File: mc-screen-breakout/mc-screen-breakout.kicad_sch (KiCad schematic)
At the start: 25 parts, among them J1 USB_C_Receptacle_PowerOnly_6P, J2 FH28-10S-0.5SH_05_, U2 MDBT50Q-1MV2, Y1 Crystal_GND24

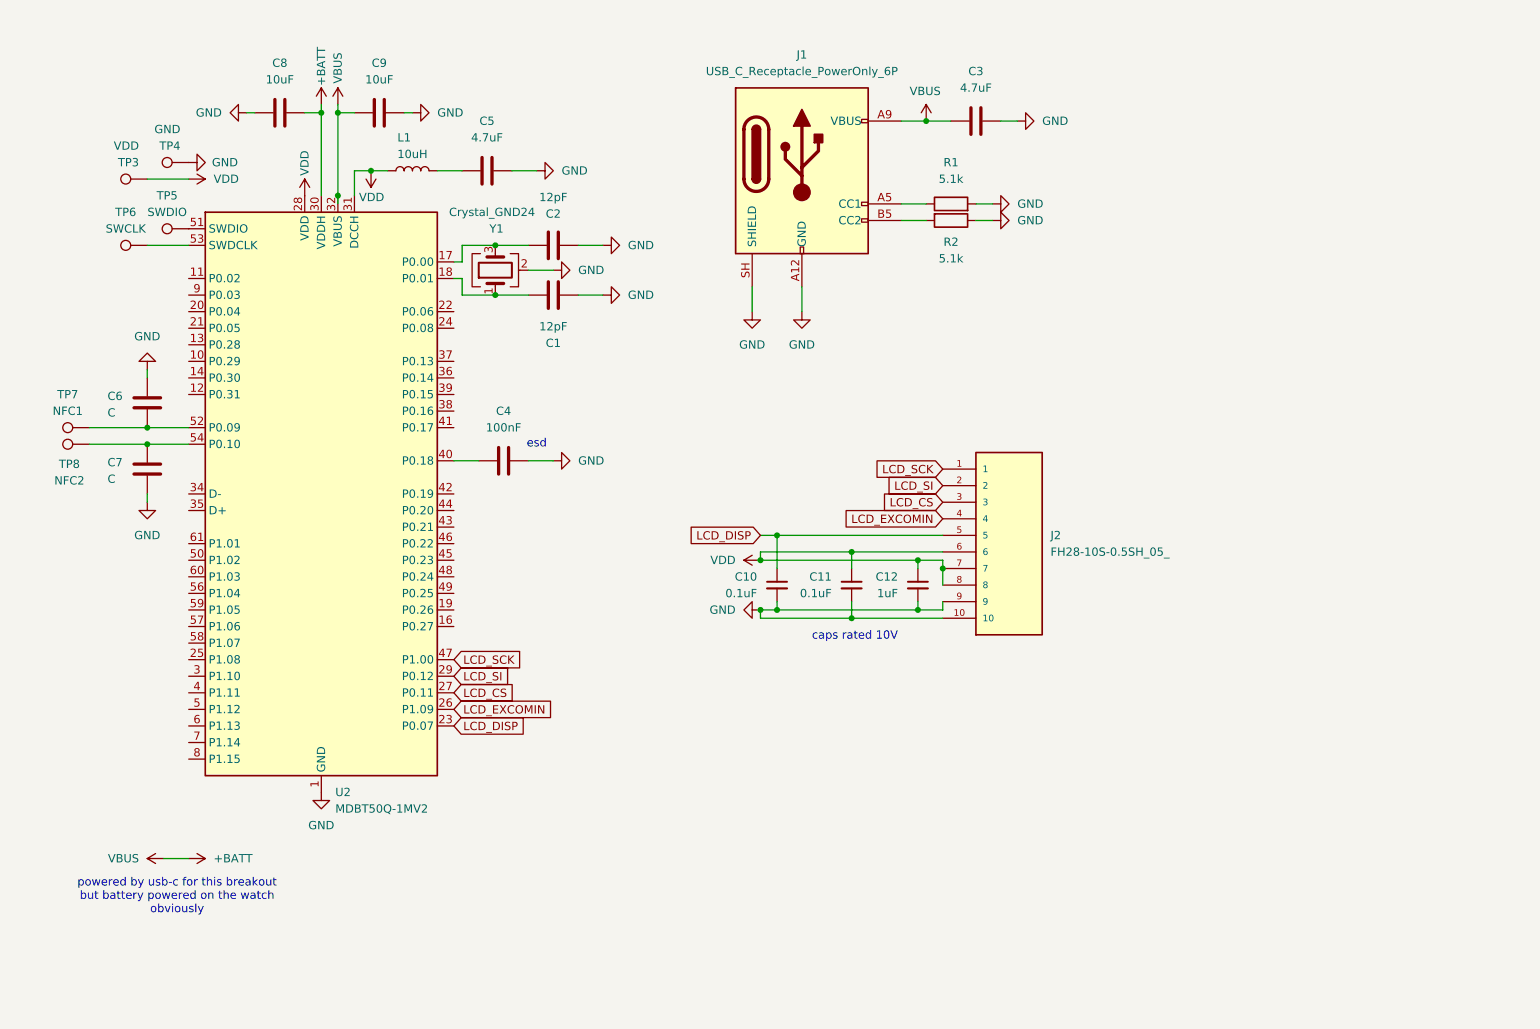
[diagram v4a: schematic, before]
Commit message: Added mic and switches
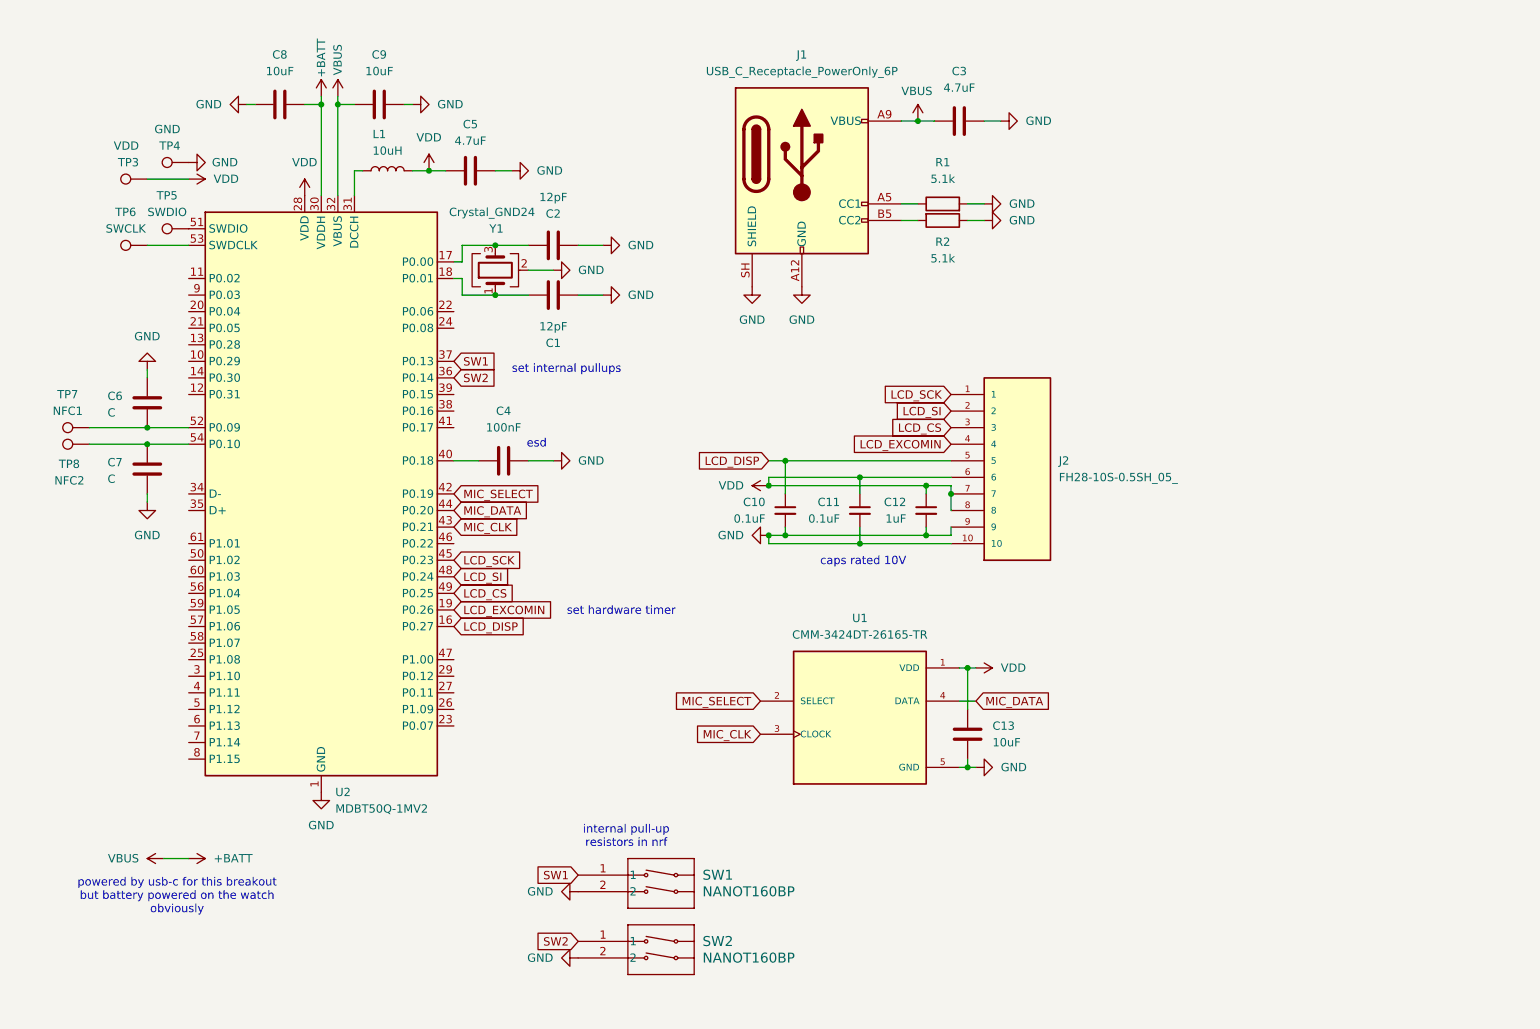
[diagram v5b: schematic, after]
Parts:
- added C13: 10uF, symbol Device:C
- added SW1, SW2: NANOT160BP, SW_NANOT160BP_CNK, symbol NANOT160BP:NANOT160BP
- added U1: CMM-3424DT-26165-TR, CMM-3424DT-26165-TR:MIC_CMM-3424DT-26165-TR, symbol CMM-3424DT-26165-TR:CMM-3424DT-26165-TR
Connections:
- net GND: now also C13.2, SW1.2, SW2.2, U1.5 (GND), U1.6 (GND), U1.7 (GND), U1.8 (GND)
- net LCD_CS: now also U2.49 (P0.25); no longer U2.27 (P0.11)
- net LCD_DISP: now also U2.16 (P0.27); no longer U2.23 (P0.07)
- net LCD_EXCOMIN: now also U2.19 (P0.26); no longer U2.26 (P1.09)
- net LCD_SCK: now also U2.45 (P0.23); no longer U2.47 (P1.00)
- net LCD_SI: now also U2.48 (P0.24); no longer U2.29 (P0.12)
- net VDD: now also C5.1, L1.2, C13.1, U1.1 (VDD); no longer L1.1, U2.31 (DCCH)
- net SW2: now reaches U2.36 (P0.14)
- net SW2: now also SW2.1
- net SW1: now reaches U2.37 (P0.13)
- net SW1: now also SW1.1
- net MIC_SELECT: now reaches U2.42 (P0.19)
- net MIC_SELECT: now also U1.2 (SELECT)
- net MIC_CLK: now reaches U2.43 (P0.21)
- net MIC_CLK: now also U1.3 (CLOCK)
- net MIC_DATA: now reaches U2.44 (P0.20)
- net MIC_DATA: now also U1.4 (DATA)
- new net: L1.1, U2.31 (DCCH)
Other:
- note added: "internal pull-up resistors in nrf"
- note added: "set hardware timer"
- note added: "set internal pullups"
- moved on the sheet: C10, C11, C12, C3, C5, C8, C9, J2, L1, R1, R2

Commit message: Schematic fixes and started routing
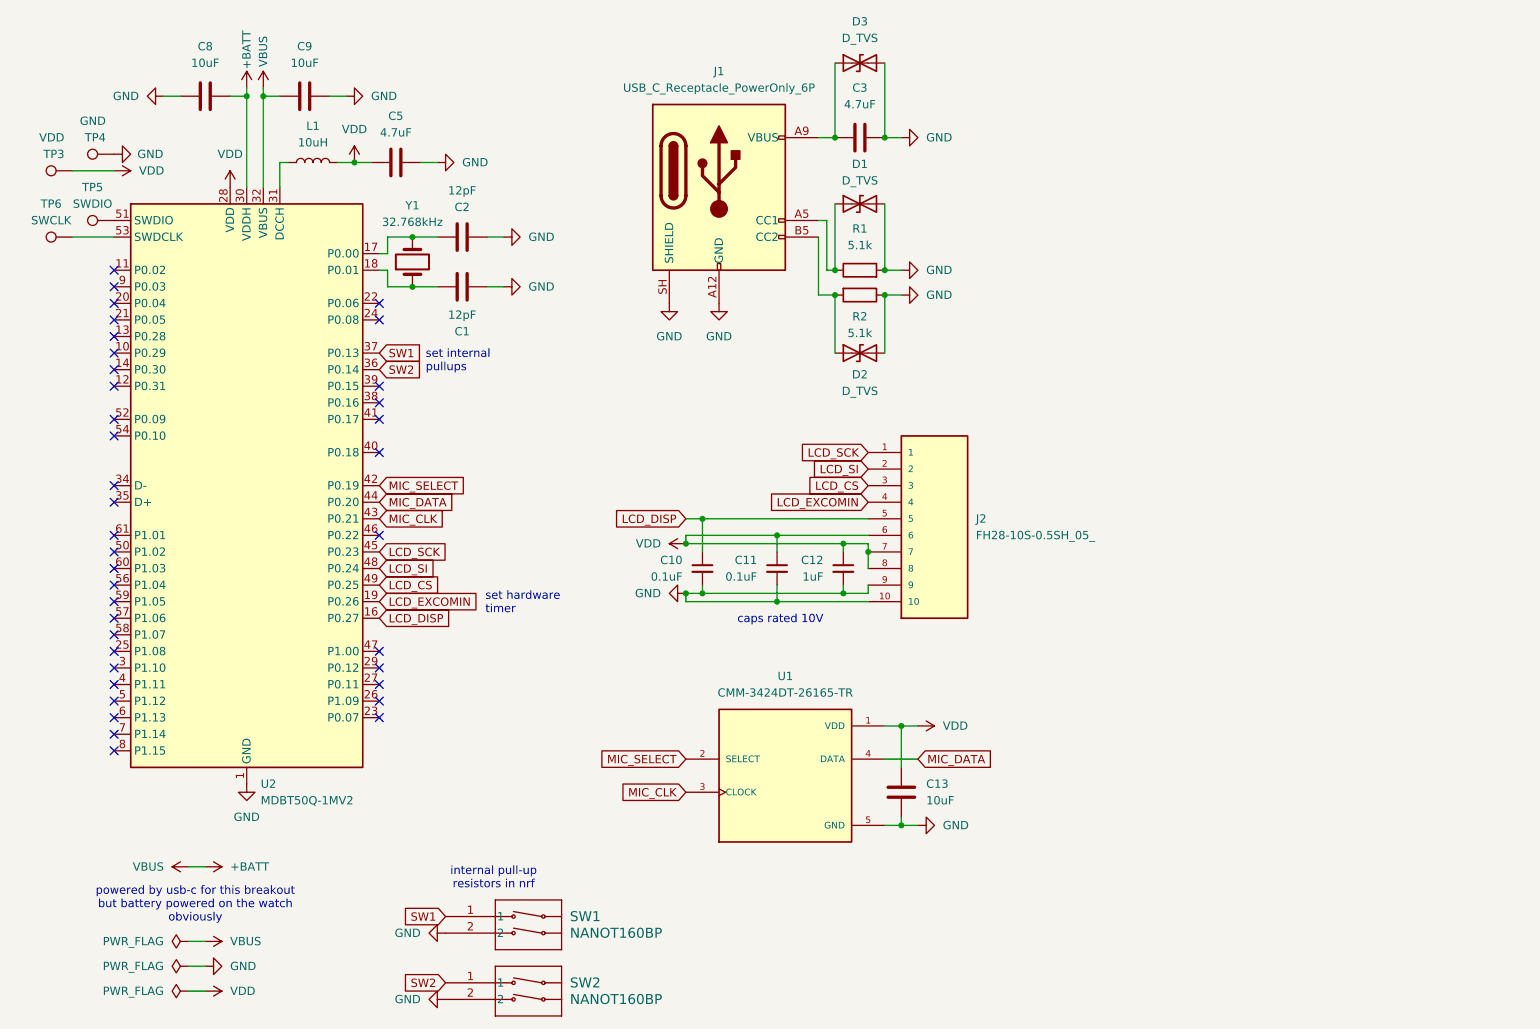
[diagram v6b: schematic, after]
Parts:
- removed C4: 100nF, symbol Device:C
- removed C6, C7: C, symbol Device:C
- removed TP7: NFC1, symbol Connector:TestPoint
- removed TP8: NFC2, symbol Connector:TestPoint
- removed Y1: Crystal_GND24, symbol Device:Crystal_GND24
- added D1, D2, D3: D_TVS, Diode_SMD:D_0402_1005Metric, symbol Device:D_TVS
- added Y1: 32.768kHz, Crystal:Crystal_SMD_3215-2Pin_3.2x1.5mm, symbol Device:Crystal
- C1, C10, C11, C12, C13, C2, C3, C5, C8, C9: footprint (none) -> Capacitor_SMD:C_0402_1005Metric
- J1: footprint (none) -> Connector_USB:USB_C_Receptacle_Amphenol_124019772112A
- L1: footprint (none) -> Inductor_SMD:L_0603_1608Metric
- R1, R2: footprint (none) -> Resistor_SMD:R_0402_1005Metric
- SW1, SW2: footprint SW_NANOT160BP_CNK -> NANOT160BP:SW_NANOT160BP_CNK
- TP3, TP4, TP5, TP6: footprint (none) -> TestPoint:TestPoint_Pad_1.0x1.0mm
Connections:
- net +BATT: no longer C3.1, J1.A9 (VBUS), J1.B9 (VBUS)
- net GND: now also D1.2 (A2), D2.2 (A2), D3.2 (A2)
- net at C2.1, U2.17 (P0.00): now also Y1.2
- net at J1.A5 (CC1), R1.1: now also D1.1 (A1)
- net at J1.B5 (CC2), R2.2: now also D2.1 (A1)
- net at C1.2, U2.18 (P0.01): now also Y1.1
- new net: C3.1, D3.1 (A1), J1.A9 (VBUS), J1.B9 (VBUS)
- no-connect marks 0 -> 38
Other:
- note removed: "esd"
- moved on the sheet: C1, C10, C11, C12, C13, C2, C3, C5, C8, C9, J1, J2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

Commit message: Began drawing traces
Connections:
- net LCD_CS: now also U2.6 (P1.13); no longer U2.49 (P0.25)
- net LCD_DISP: now also U2.8 (P1.15); no longer U2.16 (P0.27)
- net LCD_EXCOMIN: now also U2.7 (P1.14); no longer U2.19 (P0.26)
- net LCD_SCK: now also U2.4 (P1.11); no longer U2.45 (P0.23)
- net LCD_SI: now also U2.5 (P1.12); no longer U2.48 (P0.24)
- net MIC_CLK: now also U2.20 (P0.04); no longer U2.43 (P0.21)
- net MIC_DATA: now also U2.21 (P0.05); no longer U2.44 (P0.20)
- net MIC_SELECT: now also U2.22 (P0.06); no longer U2.42 (P0.19)
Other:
- note added: "set hardware timer excom"
- note removed: "set hardware timer"
- moved on the sheet: C1, C2, C5, C8, C9, L1, TP3, TP4, TP5, TP6, U2, Y1

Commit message: More routing
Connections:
- net LCD_CS: now also U2.8 (P1.15); no longer U2.6 (P1.13)
- net LCD_DISP: now also U2.13 (P0.28); no longer U2.8 (P1.15)
- net LCD_EXCOMIN: now also U2.14 (P0.30); no longer U2.7 (P1.14)
- net LCD_SI: now also U2.6 (P1.13); no longer U2.5 (P1.12)
